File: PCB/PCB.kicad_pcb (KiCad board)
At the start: 2 copper layers, 130.8 x 85.1 mm, 49 parts, among them J1 Conn_01x04_Female, J10 Conn_01x08_Female, J11 Conn_01x01_Female, J12 Conn_01x04_Female, J2 Conn_01x28_Female, J3 Conn_01x02_Female, J4 Conn_01x02_Female, J5 Conn_01x02_Female, J6 Conn_01x02_Female, J7 Conn_01x08_Female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

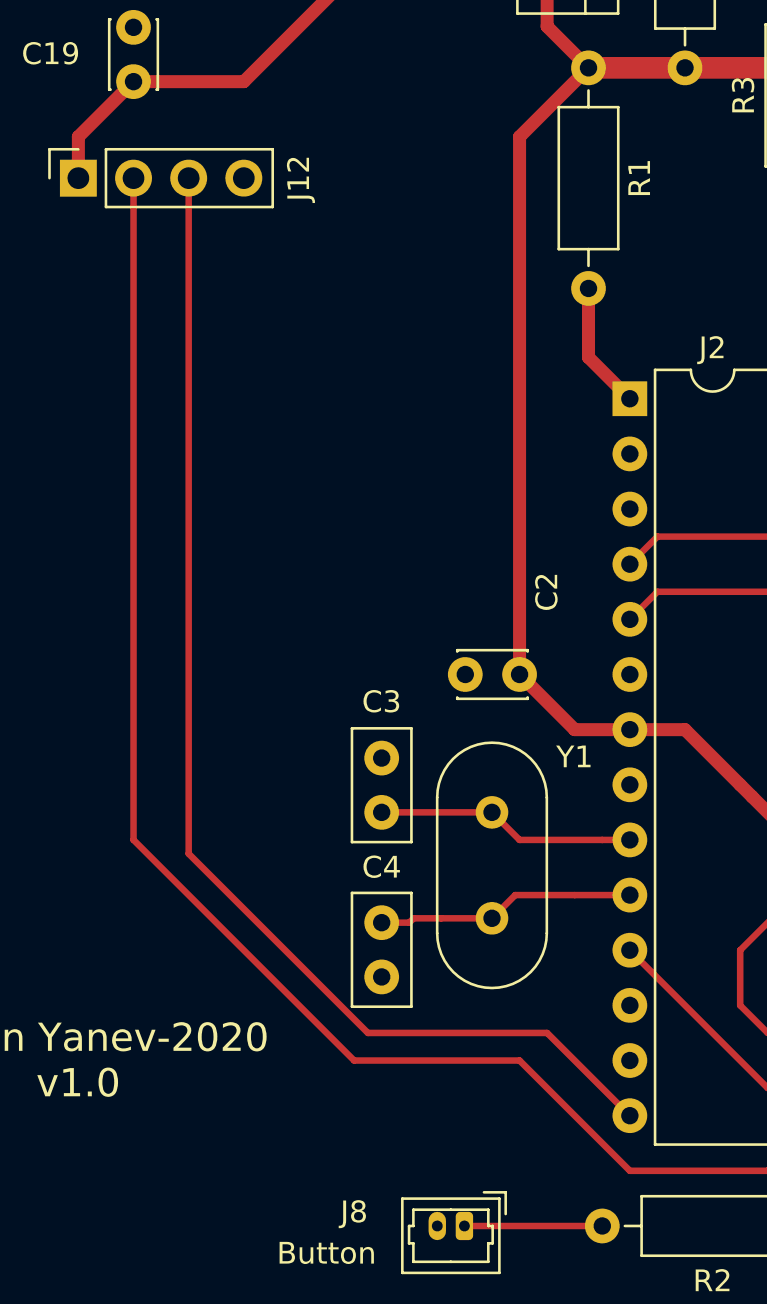
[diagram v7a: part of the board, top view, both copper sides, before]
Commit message: Moved Crystal Capacitors
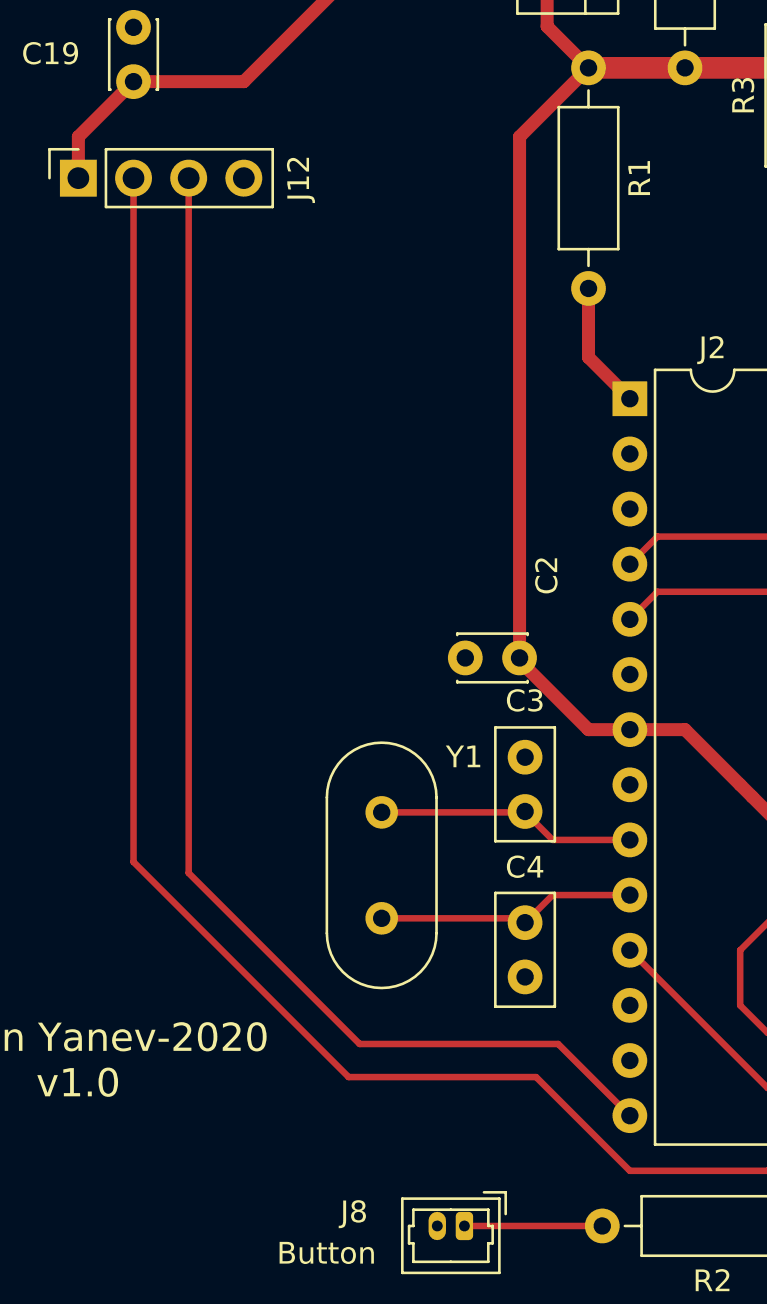
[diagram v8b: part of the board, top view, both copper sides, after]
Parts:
- moved C3 6.60 mm to (104.4, 77.5)
- moved C4 6.60 mm to (104.4, 85.1)
- moved Y1 5.08 mm to (97.8, 80.0)
- moved C2 0.76 mm to (104.1, 72.9)
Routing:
- net TX: track 69.1 -> 69.7 mm
- net RX: track 56.4 -> 57.0 mm
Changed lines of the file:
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@@
     (thickness 1.6)
     (drawings 20)
-    (tracks 164)
+    (tracks 158)
     (zones 0)
     (modules 49)
@@
   )
   (module Capacitor_THT:C_Disc_D3.0mm_W2.0mm_P2.50mm (layer F.Cu)
-    (at 104.14 73.66 180)
+    (at 104.14 72.898 180)
     (descr "C, Disc series, Radial, pin pitch=2.50mm, , diameter*width=3*2mm^2, Capacitor")
     (tags "C Disc series Radial pin pitch 2.50mm  diameter 3mm width 2mm Capacitor")
@@
   )
   (module Capacitor_THT:C_Disc_D5.0mm_W2.5mm_P2.50mm (layer F.Cu)
-    (at 97.79 77.51 270)
+    (at 104.394 77.47 270)
     (descr "C, Disc series, Radial, pin pitch=2.50mm, , diameter*width=5*2.5mm^2, Capacitor, http://cdn-reichelt.de/documents/datenblatt/B300/DS_KERKO_TC.pdf")
     (tags "C Disc series Radial pin pitch 2.50mm  diameter 5mm width 2.5mm Capacitor")
@@
   )
   (module Capacitor_THT:C_Disc_D5.0mm_W2.5mm_P2.50mm (layer F.Cu)
-    (at 97.79 85.09 270)
+    (at 104.394 85.09 270)
     (descr "C, Disc series, Radial, pin pitch=2.50mm, , diameter*width=5*2.5mm^2, Capacitor, http://cdn-reichelt.de/documents/datenblatt/B300/DS_KERKO_TC.pdf")
     (tags "C Disc series Radial pin pitch 2.50mm  diameter 5mm width 2.5mm Capacitor")
@@
   )
   (module Crystal:Crystal_HC49-U_Vertical (layer F.Cu)
-    (at 102.87 80.01 270)
+    (at 97.79 80.01 270)
     (descr "Crystal THT HC-49/U http://5hertz.com/pdfs/04404_D.pdf")
     (tags "THT crystalHC-49/U")
@@
   (segment (start 117.475 81.915) (end 116.84 81.28) (width 0.6) (layer F.Cu) (net 3))
   (segment (start 120.65 81.915) (end 117.475 81.915) (width 0.6) (layer F.Cu) (net 3))
-  (segment (start 109.22 76.2) (end 106.68 76.2) (width 0.6) (layer F.Cu) (net 3))
-  (segment (start 106.68 76.2) (end 104.14 73.66) (width 0.6) (layer F.Cu) (net 3))
   (segment (start 105.41 43.815) (end 105.41 40.64) (width 0.6) (layer F.Cu) (net 3))
   (segment (start 107.315 45.72) (end 105.41 43.815) (width 0.6) (layer F.Cu) (net 3))
-  (segment (start 104.14 73.66) (end 104.14 48.895) (width 0.6) (layer F.Cu) (net 3))
-  (segment (start 104.14 48.895) (end 107.315 45.72) (width 0.6) (layer F.Cu) (net 3))
   (segment (start 141.605 52.07) (end 141.605 38.1) (width 1) (layer F.Cu) (net 3))
   (segment (start 141.605 38.1) (end 140.335 36.83) (width 1) (layer F.Cu) (net 3))
@@
   (segment (start 140.335 36.83) (end 130.175 36.83) (width 1) (layer F.Cu) (net 3))
   (segment (start 130.175 36.83) (end 121.285 45.72) (width 1) (layer F.Cu) (net 3))
-  (segment (start 109.22 81.28) (end 107.95 81.28) (width 0.3) (layer F.Cu) (net 4))
-  (segment (start 107.95 81.28) (end 104.14 81.28) (width 0.3) (layer F.Cu) (net 4))
-  (segment (start 104.14 81.28) (end 102.87 80.01) (width 0.3) (layer F.Cu) (net 4))
-  (segment (start 102.87 80.01) (end 97.79 80.01) (width 0.3) (layer F.Cu) (net 4))
-  (segment (start 102.87 84.89) (end 100.53 84.89) (width 0.3) (layer F.Cu) (net 5))
-  (segment (start 99.26 84.89) (end 99.06 85.09) (width 0.3) (layer F.Cu) (net 5))
-  (segment (start 99.06 85.09) (end 97.79 85.09) (width 0.3) (layer F.Cu) (net 5))
-  (segment (start 100.53 84.89) (end 99.26 84.89) (width 0.3) (layer F.Cu) (net 5))
-  (segment (start 106.68 83.82) (end 106.48 83.82) (width 0.25) (layer F.Cu) (net 5))
-  (segment (start 109.22 83.82) (end 106.68 83.82) (width 0.3) (layer F.Cu) (net 5))
-  (segment (start 103.94 83.82) (end 102.87 84.89) (width 0.3) (layer F.Cu) (net 5))
-  (segment (start 106.68 83.82) (end 103.94 83.82) (width 0.3) (layer F.Cu) (net 5))
+  (segment (start 104.14 48.895) (end 107.315 45.72) (width 0.6) (layer F.Cu) (net 3))
+  (segment (start 104.14 73.025) (end 104.14 48.895) (width 0.6) (layer F.Cu) (net 3))
+  (segment (start 109.22 76.2) (end 107.315 76.2) (width 0.6) (layer F.Cu) (net 3))
+  (segment (start 107.315 76.2) (end 104.14 73.025) (width 0.6) (layer F.Cu) (net 3))
+  (segment (start 104.394 80.01) (end 97.79 80.01) (width 0.3) (layer F.Cu) (net 4))
+  (segment (start 109.22 81.28) (end 105.664 81.28) (width 0.3) (layer F.Cu) (net 4))
+  (segment (start 105.664 81.28) (end 104.394 80.01) (width 0.3) (layer F.Cu) (net 4))
+  (segment (start 104.594 84.89) (end 97.79 84.89) (width 0.3) (layer F.Cu) (net 5))
+  (segment (start 109.22 83.82) (end 105.664 83.82) (width 0.3) (layer F.Cu) (net 5))
+  (segment (start 105.664 83.82) (end 104.594 84.89) (width 0.3) (layer F.Cu) (net 5))
   (segment (start 119.38 78.74) (end 120.65 77.47) (width 0.6) (layer F.Cu) (net 6))
   (segment (start 116.84 78.74) (end 119.38 78.74) (width 0.6) (layer F.Cu) (net 6))
@@
   (segment (start 107.315 59.055) (end 109.22 60.96) (width 0.6) (layer F.Cu) (net 11))
   (segment (start 107.315 55.88) (end 107.315 59.055) (width 0.6) (layer F.Cu) (net 11))
-  (segment (start 88.9 81.915) (end 88.9 50.8) (width 0.3) (layer F.Cu) (net 12))
-  (segment (start 97.155 90.17) (end 88.9 81.915) (width 0.3) (layer F.Cu) (net 12))
-  (segment (start 109.22 93.98) (end 105.41 90.17) (width 0.3) (layer F.Cu) (net 12))
-  (segment (start 105.41 90.17) (end 97.155 90.17) (width 0.3) (layer F.Cu) (net 12))
+  (segment (start 88.9 82.804) (end 88.9 50.8) (width 0.3) (layer F.Cu) (net 12))
+  (segment (start 96.774 90.678) (end 88.9 82.804) (width 0.3) (layer F.Cu) (net 12))
+  (segment (start 109.22 93.98) (end 105.918 90.678) (width 0.3) (layer F.Cu) (net 12))
+  (segment (start 105.918 90.678) (end 96.774 90.678) (width 0.3) (layer F.Cu) (net 12))
   (segment (start 121.92 91.44) (end 116.84 91.44) (width 0.3) (layer F.Cu) (net 13))
   (segment (start 123.952 91.44) (end 128.27 87.122) (width 0.3) (layer F.Cu) (net 13))
@@
   (segment (start 129.794 74.422) (end 137.933529 74.422) (width 0.3) (layer F.Cu) (net 13))
   (segment (start 137.933529 74.422) (end 139.4587 75.947171) (width 0.3) (layer F.Cu) (net 13))
-  (segment (start 86.36 81.28) (end 86.36 50.8) (width 0.3) (layer F.Cu) (net 14))
-  (segment (start 96.52 91.44) (end 86.36 81.28) (width 0.3) (layer F.Cu) (net 14))
-  (segment (start 104.14 91.44) (end 96.52 91.44) (width 0.3) (layer F.Cu) (net 14))
-  (segment (start 115.57 96.52) (end 109.22 96.52) (width 0.3) (layer F.Cu) (net 14))
-  (segment (start 109.22 96.52) (end 104.14 91.44) (width 0.3) (layer F.Cu) (net 14))
-  (segment (start 116.84 93.98) (end 116.84 95.25) (width 0.3) (layer F.Cu) (net 14))
+  (segment (start 86.36 82.296) (end 86.36 50.8) (width 0.3) (layer F.Cu) (net 14))
   (segment (start 116.84 95.25) (end 115.57 96.52) (width 0.3) (layer F.Cu) (net 14))
+  (segment (start 116.84 93.98) (end 116.84 95.25) (width 0.3) (layer F.Cu) (net 14))
+  (segment (start 115.57 96.52) (end 109.22 96.52) (width 0.3) (layer F.Cu) (net 14))
+  (segment (start 109.22 96.52) (end 104.902 92.202) (width 0.3) (layer F.Cu) (net 14))
+  (segment (start 104.902 92.202) (end 96.266 92.202) (width 0.3) (layer F.Cu) (net 14))
+  (segment (start 96.266 92.202) (end 86.36 82.296) (width 0.3) (layer F.Cu) (net 14))
   (segment (start 120.65 88.9) (end 116.84 88.9) (width 0.3) (layer F.Cu) (net 15))
   (segment (start 121.412 88.9) (end 126.238 84.074) (width 0.3) (layer F.Cu) (net 15))
